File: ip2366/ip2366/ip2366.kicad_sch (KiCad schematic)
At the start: 12 parts, among them CN1 XT30PW-M, Q1 RU3030M2-VB, U1 IP2366 (I2C VERSION)

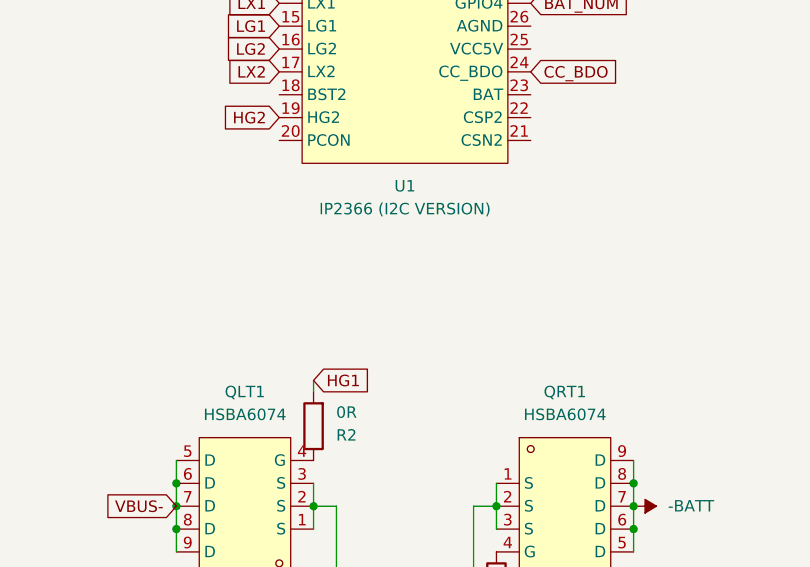
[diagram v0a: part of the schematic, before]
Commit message: add some components
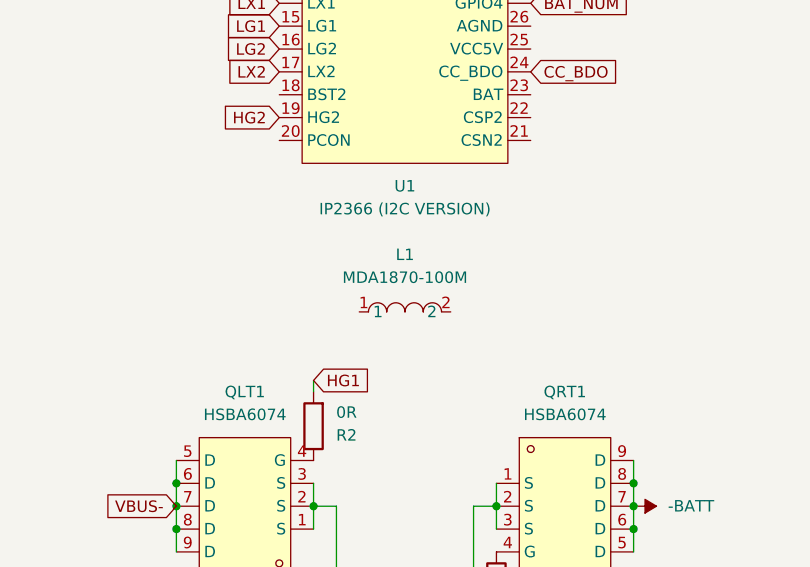
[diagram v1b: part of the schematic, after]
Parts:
- added L1: MDA1870-100M, easyeda2kicad:IND-SMD_2P-L16.9-W16.9, symbol easyeda2kicad:MDA1870-100M
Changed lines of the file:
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@@
+	)
+	(symbol
+		(lib_id "easyeda2kicad:MDA1870-100M")
+		(at 135.89 123.19 0)
+		(unit 1)
+		(exclude_from_sim no)
+		(in_bom yes)
+		(on_board yes)
+		(dnp no)
+		(fields_autoplaced yes)
+		(property "Reference" "L1"
+			(at 135.89 116.84 0)
+			(effects
+				(font
+					(size 1.27 1.27)
+				)
+			)
+		)
+		(property "Value" "MDA1870-100M"
+			(at 135.89 119.38 0)
+			(effects
+				(font
+					(size 1.27 1.27)
+				)
+			)
+		)
+		(property "Footprint" "easyeda2kicad:IND-SMD_2P-L16.9-W16.9"
+			(at 135.89 130.81 0)
+			(effects
+				(font
+					(size 1.27 1.27)
+				)
+				(hide yes)
+			)
+		)
+		(property "Datasheet" ""
+			(at 135.89 123.19 0)
+			(effects
+				(font
+					(size 1.27 1.27)
+				)
+				(hide yes)
+			)
+		)
+		(property "Description" ""
+			(at 135.89 123.19 0)
+			(effects
+				(font
+					(size 1.27 1.27)
+				)
+				(hide yes)
+			)
+		)
+		(property "LCSC Part" "C2847588"
+			(at 135.89 133.35 0)
+			(effects
+				(font
+					(size 1.27 1.27)
+				)
+				(hide yes)
+			)
+		)
+		(pin "2"
+		)
+		(pin "1"
+		)
+		(instances
+			(project ""
+				(path "/2ca5f6a3-9021-4596-b870-f2bf74885223"
+					(reference "L1")
+					(unit 1)
+				)
+			)
+		)
 	)
 	(symbol

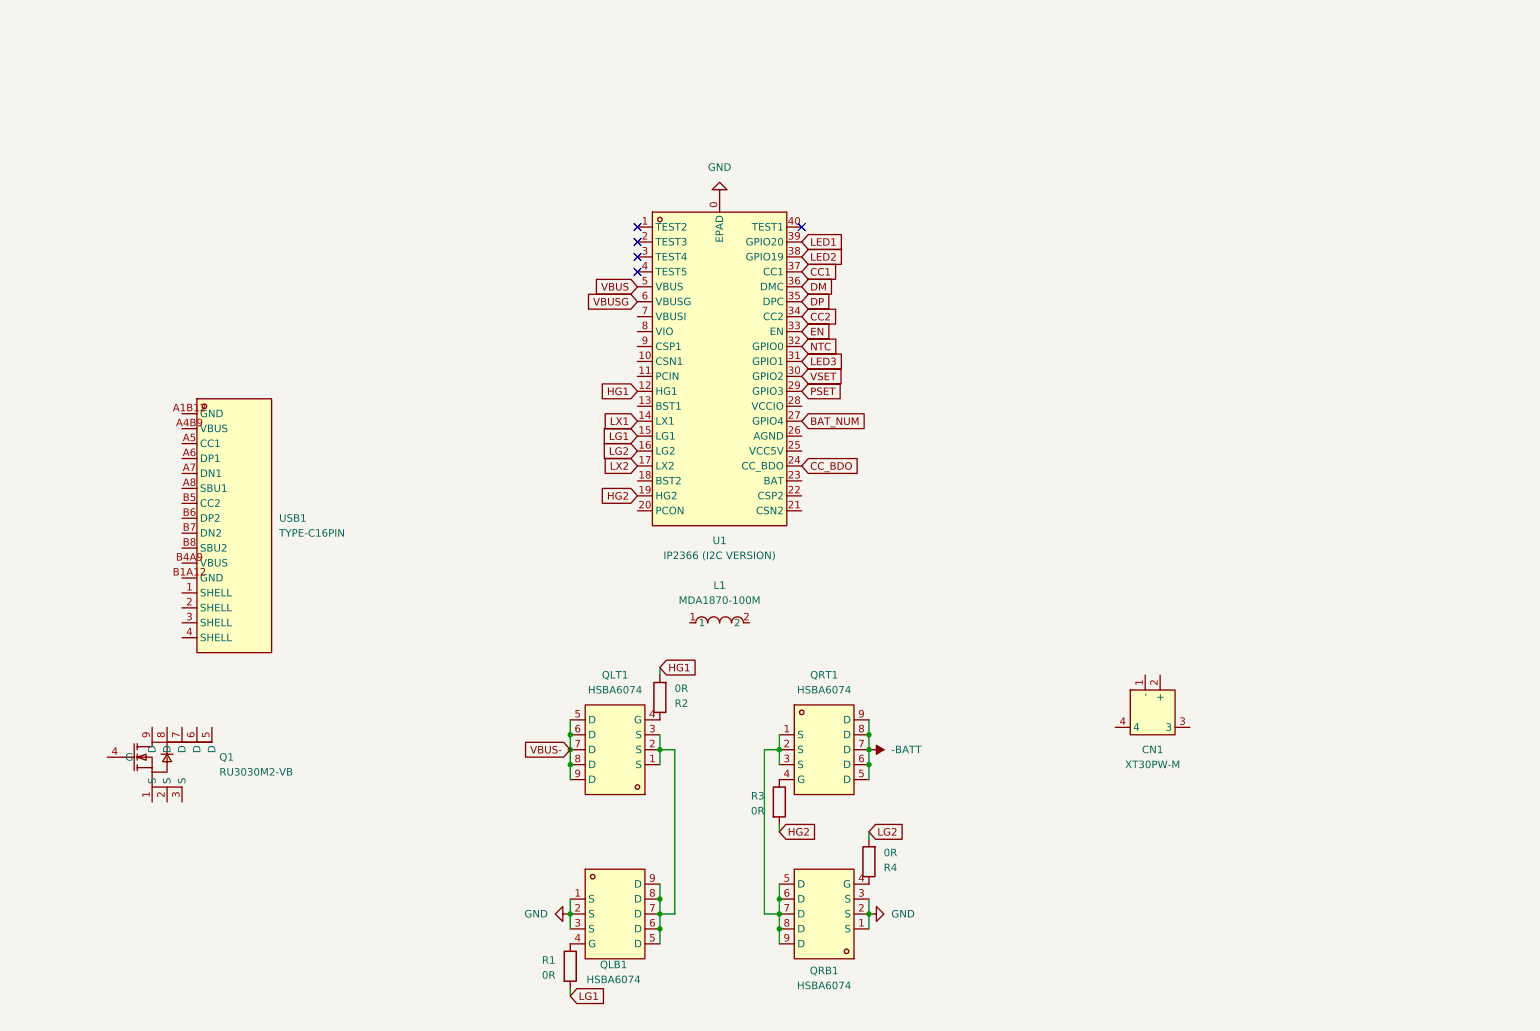
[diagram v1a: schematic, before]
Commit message: add some more components
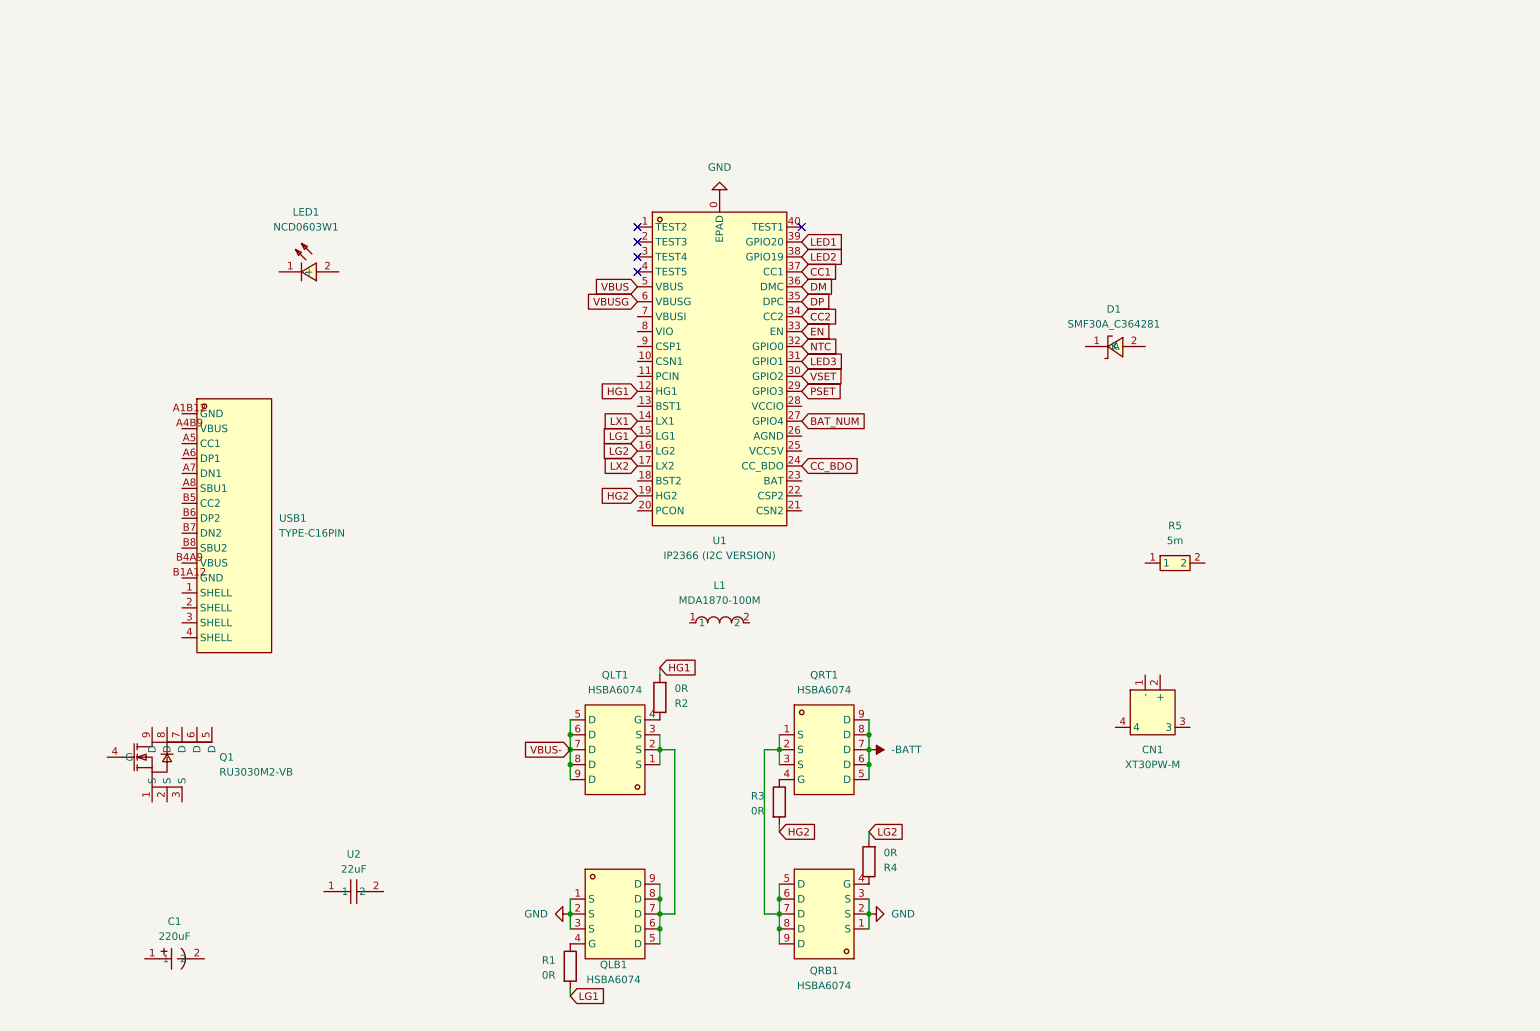
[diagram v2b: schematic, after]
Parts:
- added C1: 220uF, easyeda2kicad:CAP-TH_BD8.0-P3.50-D0.6-FD, symbol easyeda2kicad:SPZ1VM221F11O00RAXXX
- added D1: SMF30A_C364281, easyeda2kicad:SOD-123_L2.6-W1.6-LS3.5-RD, symbol easyeda2kicad:SMF30A_C364281
- added LED1: NCD0603W1, easyeda2kicad:LED0603-RD, symbol easyeda2kicad:NCD0603W1
- added R5: 5m, easyeda2kicad:R1206, symbol easyeda2kicad:FRM121WFR005TM
- added U2: 22uF, easyeda2kicad:C1210, symbol easyeda2kicad:GMK325BJ226MM-P

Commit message: add balancing board
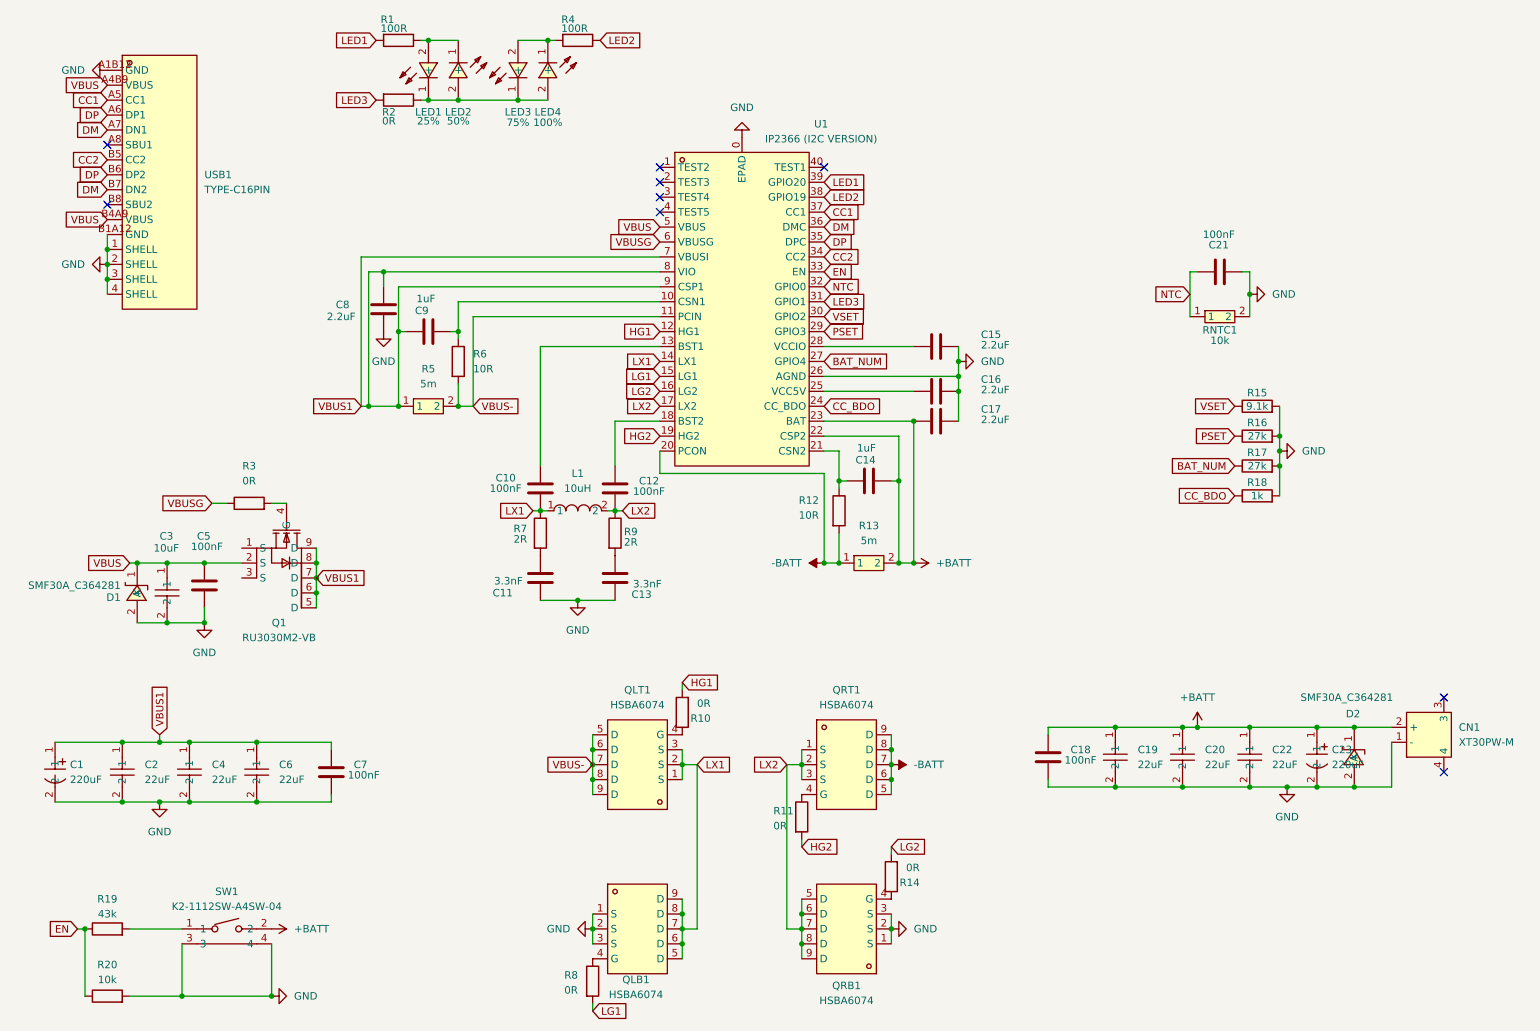
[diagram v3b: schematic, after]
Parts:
- added C10, C12, C18, C21, C5, C7: 100nF, Capacitor_SMD:C_0603_1608Metric_Pad1.08x0.95mm_HandSolder, symbol Device:C
- added C11, C13: 3.3nF, Capacitor_SMD:C_0603_1608Metric_Pad1.08x0.95mm_HandSolder, symbol Device:C
- added C14, C9: 1uF, Capacitor_SMD:C_0603_1608Metric_Pad1.08x0.95mm_HandSolder, symbol Device:C
- added C15, C16, C17, C8: 2.2uF, Capacitor_SMD:C_0603_1608Metric_Pad1.08x0.95mm_HandSolder, symbol Device:C
- added C19, C20, C22, C4, C6: 22uF, easyeda2kicad:C1210, symbol easyeda2kicad:GMK325BJ226MM-P
- added C23: 220uF, easyeda2kicad:CAP-TH_BD8.0-P3.50-D0.6-FD, symbol easyeda2kicad:SPZ1VM221F11O00RAXXX
- added C3: 10uF, easyeda2kicad:C1206, symbol easyeda2kicad:CL31B106KBHNNNE
- added D2: SMF30A_C364281, easyeda2kicad:SOD-123_L2.6-W1.6-LS3.5-RD, symbol easyeda2kicad:SMF30A_C364281
- added LED2: 50%, easyeda2kicad:LED0603-RD, symbol easyeda2kicad:NCD0603W1
- added LED3: 75%, easyeda2kicad:LED0603-RD, symbol easyeda2kicad:NCD0603W1
- added LED4: 100%, easyeda2kicad:LED0603-RD, symbol easyeda2kicad:NCD0603W1
- added R1, R4: 100R, Resistor_SMD:R_0603_1608Metric_Pad0.98x0.95mm_HandSolder, symbol Device:R
- added R12: 10R, Capacitor_SMD:C_0603_1608Metric_Pad1.08x0.95mm_HandSolder, symbol Device:R
- added R13: 5m, Resistor_SMD:R_2512_6332Metric_Pad1.40x3.35mm_HandSolder, symbol easyeda2kicad:FRM121WFR005TM
- added R15: 9.1k, Resistor_SMD:R_0603_1608Metric_Pad0.98x0.95mm_HandSolder, symbol Device:R
- added R16, R17: 27k, Resistor_SMD:R_0603_1608Metric_Pad0.98x0.95mm_HandSolder, symbol Device:R
- added R18: 1k, Resistor_SMD:R_0603_1608Metric_Pad0.98x0.95mm_HandSolder, symbol Device:R
- added R19: 43k, Resistor_SMD:R_0603_1608Metric_Pad0.98x0.95mm_HandSolder, symbol Device:R
- added R2, R3: 0R, Resistor_SMD:R_0603_1608Metric_Pad0.98x0.95mm_HandSolder, symbol Device:R
- added R20: 10k, Resistor_SMD:R_0603_1608Metric_Pad0.98x0.95mm_HandSolder, symbol Device:R
- added R6: 10R, Resistor_SMD:R_0603_1608Metric_Pad0.98x0.95mm_HandSolder, symbol Device:R
- added R7, R9: 2R, Resistor_SMD:R_0603_1608Metric_Pad0.98x0.95mm_HandSolder, symbol Device:R
- added RNTC1: 10k, easyeda2kicad:R0603, symbol easyeda2kicad:RC0603FR-0710KL
- added SW1: K2-1112SW-A4SW-04, easyeda2kicad:KEY-TH_K2-1112SW-AXXW-XX, symbol easyeda2kicad:K2-1112SW-A4SW-04
- L1: value MDA1870-100M -> 10uH
- LED1: value NCD0603W1 -> 25%
- R10: renamed from R2; footprint (none) -> Resistor_SMD:R_0603_1608Metric_Pad0.98x0.95mm_HandSolder
- R11: renamed from R3; footprint (none) -> Resistor_SMD:R_0603_1608Metric_Pad0.98x0.95mm_HandSolder
- R14: renamed from R4; footprint (none) -> Resistor_SMD:R_0603_1608Metric_Pad0.98x0.95mm_HandSolder
- R5: footprint easyeda2kicad:R1206 -> Resistor_SMD:R_2512_6332Metric_Pad1.40x3.35mm_HandSolder; LCSC Part C7419996 -> C5123656
- R8: renamed from R1; footprint (none) -> Resistor_SMD:R_0603_1608Metric_Pad0.98x0.95mm_HandSolder
- renumbered U2 to C2
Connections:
- net -BATT: now also U1.20 (PCON), R12.2, R13.1
- net BAT_NUM: now also R17.1
- net CC1: now also USB1.A5 (CC1)
- net CC2: now also USB1.B5 (CC2)
- net CC_BDO: now also R18.1
- net DM: now also USB1.A7 (DN1), USB1.B7 (DN2)
- net DP: now also USB1.A6 (DP1), USB1.B6 (DP2)
- net EN: now also R19.1, R20.1
- net GND: now also C1.2, C2.2, CN1.1 (-), D1.2 (A), U1.26 (AGND), USB1.1 (SHELL), USB1.2 (SHELL), USB1.3 (SHELL), USB1.4 (SHELL), USB1.A1B12 (GND), USB1.B1A12 (GND), C11.2, C13.2, C15.1, C16.1, C17.1, C18.2, C19.2, C20.2, C21.2, C22.2, C23.2, C3.2, C4.2, C5.2, C6.2, C7.2, C8.2, D2.2 (A), R15.2, R16.2, R17.2, R18.2, R20.2, RNTC1.2, SW1.3, SW1.4
- net LED1: now also R1.2
- net LED2: now also R4.1
- net LED3: now also R2.2
- net LX1: now also L1.1, QLB1.5 (D), QLB1.6 (D), QLB1.7 (D), QLB1.8 (D), QLB1.9 (D), QLT1.1 (S), QLT1.2 (S), QLT1.3 (S), C10.2, R7.1
- net LX2: now also L1.2, QRB1.5 (D), QRB1.6 (D), QRB1.7 (D), QRB1.8 (D), QRB1.9 (D), QRT1.1 (S), QRT1.2 (S), QRT1.3 (S), C12.2, R9.1
- net NTC: now also C21.1, RNTC1.1
- net PSET: now also R16.1
- net VBUS: now also D1.1 (K), Q1.2 (S), USB1.A4B9 (VBUS), USB1.B4A9 (VBUS), C3.1, C5.1
- net VBUS-: now also R5.2, U1.11 (PCIN), R6.2
- net VBUSG: now also R3.1
- net VSET: now also R15.1
- net at U1.10 (CSN1): now also C9.1, R6.1
- net at U1.13 (BST1): now also C10.1
- net at U1.18 (BST2): now also C12.1
- net at U1.21 (CSN2): now also C14.2, R12.1
- net +BATT: now reaches U1.22 (CSP2)
- net +BATT: now also CN1.2 (+), U1.23 (BAT), C14.1, C17.2, C18.1, C19.1, C20.1, C22.1, C23.1, D2.1 (K), R13.2, SW1.2
- net at U1.25 (VCC5V): now also C16.2
- net at U1.28 (VCCIO): now also C15.2
- net VBUS1: now reaches U1.7 (VBUSI)
- net VBUS1: now also C1.1, C2.1, Q1.5 (D), Q1.6 (D), Q1.7 (D), Q1.8 (D), Q1.9 (D), R5.1, U1.8 (VIO), U1.9 (CSP1), C4.1, C6.1, C7.1, C8.1, C9.2
- net at Q1.4 (G): now also R3.2
- net at LED1.1 (-): now also LED2.2 (+), LED3.1 (-), LED4.2 (+), R2.1
- net at LED1.2 (+): now also LED2.1 (-), R1.1
- new net: LED3.2 (+), LED4.1 (-), R4.2
- new net: R19.2, SW1.1
- new net: C11.1, R7.2
- new net: C13.1, R9.2
- no-connect marks 5 -> 9
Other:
- moved on the sheet: C1, C2, CN1, D1, L1, LED1, Q1, QLB1, QLT1, QRB1, QRT1, R10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

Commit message: replace the inductor
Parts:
- removed L1: 10uH, easyeda2kicad:IND-SMD_2P-L16.9-W16.9, symbol easyeda2kicad:MDA1870-100M
- added L1: 10uH, easyeda2kicad:IND-SMD_L13.5-W12.5, symbol easyeda2kicad:SRP1265A-100M
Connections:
- net LX1: now also L1.1
- net LX2: now also L1.2
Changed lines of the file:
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@@
+	)
+	(symbol
+		(lib_id "easyeda2kicad:SRP1265A-100M")
+		(at 111.76 104.14 0)
+		(unit 1)
+		(exclude_from_sim no)
+		(in_bom yes)
+		(on_board yes)
+		(dnp no)
+		(fields_autoplaced yes)
+		(property "Reference" "L1"
+			(at 111.76 97.79 0)
+			(effects
+				(font
+					(size 1.27 1.27)
+				)
+			)
+		)
+		(property "Value" "10uH"
+			(at 111.76 100.33 0)
+			(effects
+				(font
+					(size 1.27 1.27)
+				)
+			)
+		)
+		(property "Footprint" "easyeda2kicad:IND-SMD_L13.5-W12.5"
+			(at 111.76 111.76 0)
+			(effects
+				(font
+					(size 1.27 1.27)
+				)
+				(hide yes)
+			)
+		)
+		(property "Datasheet" ""
+			(at 111.76 104.14 0)
+			(effects
+				(font
+					(size 1.27 1.27)
+				)
+				(hide yes)
+			)
+		)
+		(property "Description" ""
+			(at 111.76 104.14 0)
+			(effects
+				(font
+					(size 1.27 1.27)
+				)
+				(hide yes)
+			)
+		)
+		(property "LCSC Part" "C840531"
+			(at 111.76 114.3 0)
+			(effects
+				(font
+					(size 1.27 1.27)
+				)
+				(hide yes)
+			)
+		)
+		(pin "2"
+		)
+		(pin "1"
+		)
+		(instances
+			(project ""
+				(path "/2ca5f6a3-9021-4596-b870-f2bf74885223"
+					(reference "L1")
+					(unit 1)
+				)
+			)
+		)
 	)
 	(symbol
@@
 					(unit 1)
 				)
-			)
-		)
-	)
-	(symbol
-		(lib_id "easyeda2kicad:MDA1870-100M")
-		(at 111.76 104.14 0)
-		(unit 1)
-		(exclude_from_sim no)
-		(in_bom yes)
-		(on_board yes)
-		(dnp no)
-		(fields_autoplaced yes)
-		(property "Reference" "L1"
-			(at 111.76 97.79 0)
-			(effects
-				(font
-					(size 1.27 1.27)
-				)
-			)
-		)
-		(property "Value" "10uH"
-			(at 111.76 100.33 0)
-			(effects
-				(font
-					(size 1.27 1.27)
-				)
-			)
-		)
-		(property "Footprint" "easyeda2kicad:IND-SMD_2P-L16.9-W16.9"
-			(at 111.76 111.76 0)
-			(effects
-				(font
-					(size 1.27 1.27)
-				)
-				(hide yes)
-			)
-		)
-		(property "Datasheet" ""
-			(at 111.76 104.14 0)
-			(effects
-				(font
-					(size 1.27 1.27)
-				)
-				(hide yes)
-			)
-		)
-		(property "Description" ""
-			(at 111.76 104.14 0)
-			(effects
-				(font
-					(size 1.27 1.27)
-				)
-				(hide yes)
-			)
-		)
-		(property "LCSC Part" "C2847588"
-			(at 111.76 114.3 0)
-			(effects
-				(font
-					(size 1.27 1.27)
-				)
-				(hide yes)
-			)
-		)
-		(pin "2"
-		)
-		(pin "1"
-		)
-		(instances
-			(project ""
-				(path "/2ca5f6a3-9021-4596-b870-f2bf74885223"
-					(reference "L1")
-					(unit 1)
-				)
